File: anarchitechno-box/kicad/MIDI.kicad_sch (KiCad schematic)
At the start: 7 parts, among them CN1 PJ-3220-Y, U5 HCPL-0631

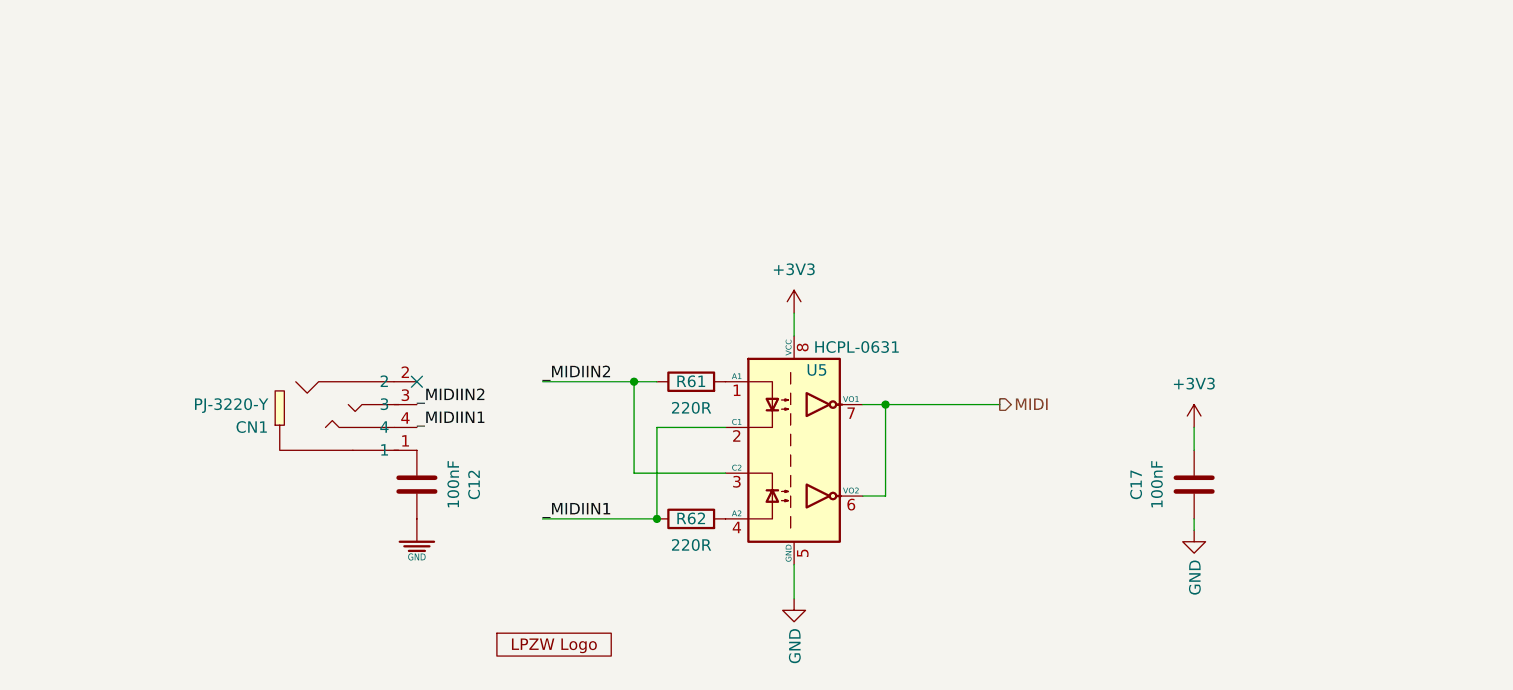
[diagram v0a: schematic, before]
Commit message: Schematic & PCB changes: - Cleaned up unnecessary electrolytic input capacitor flyback - Removed dual diode rectification on 5V, increased output capacitors - Feedback resistors DC/DCs set, enlarged for JLC basic parts - Sweep through schematic to consolidate caps to JLC basic parts (see list schematic front page) - Midi OUTPUT added (please check schematic) - Wiznet W5500 schematic reworked to RJ45 reference schematic: https://docs.wiznet.io/assets/files/w5500_sch_v110_use_mag_-dfff8bbb103d13be4f25cd2b2f8b950d.pdf - Replaced ethernet jack to HR911105A - Crystals chosen for W5500 and RP2350B (according to reference), 15pF load caps. - RS485 driver changed to SP3485EN for 3.3V operation - Replaced RS485 bus connectors with 2x RJ45s for passthrough - Groove connector replaced with JST XH 2mm - Added LCSC part numbers for various components in the schematic
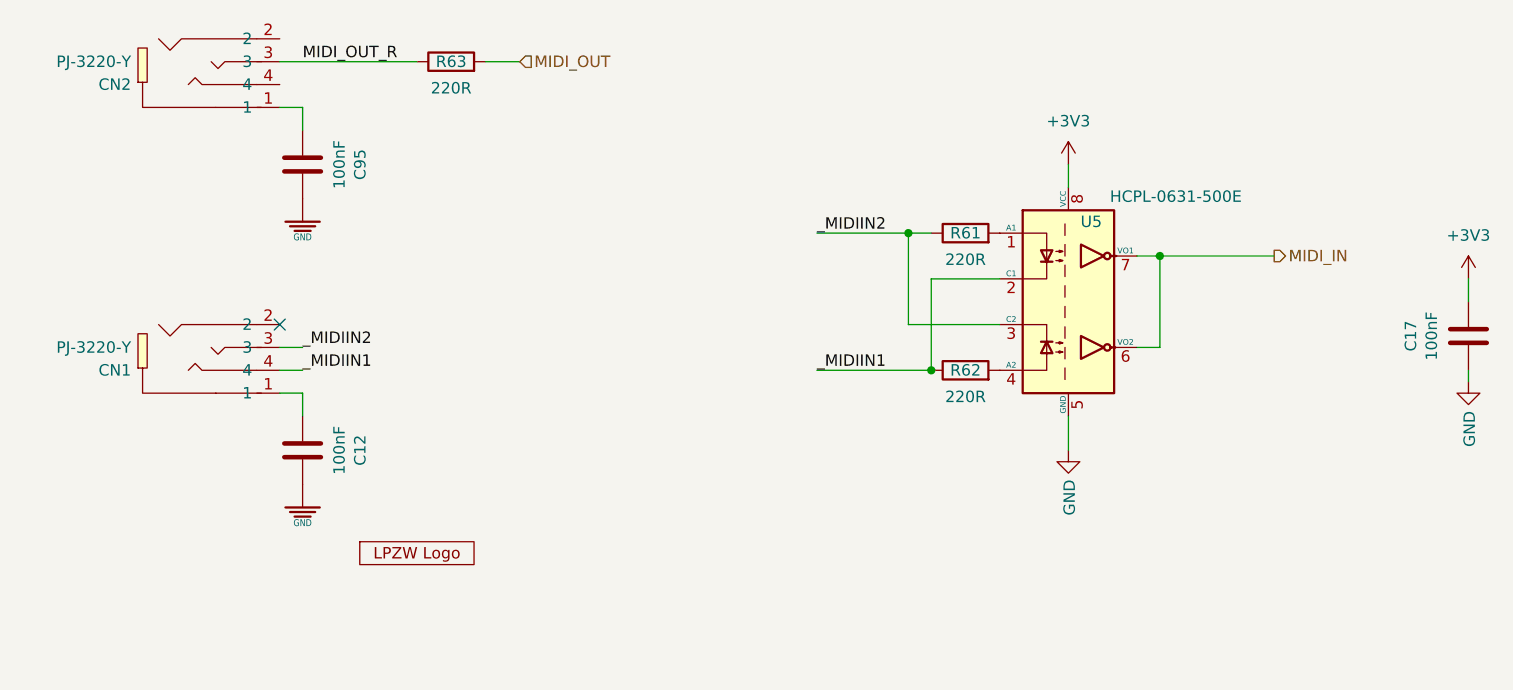
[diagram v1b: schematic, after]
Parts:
- added C95: 100nF, Capacitor_SMD:C_0402_1005Metric, symbol Device:C
- added CN2: PJ-3220-Y, parts:AUDIO-TH_PJ-3220-Y, symbol jlcpcb:PJ-3220-Y
- added R63: 220R, Resistor_SMD:R_0603_1608Metric, symbol Device:R
- CN1: footprint jlcpcb:AUDIO-TH_PJ-3220-Y -> parts:AUDIO-TH_PJ-3220-Y
- R61, R62: LCSC Part (none) -> C22962
- U5: value HCPL-0631 -> HCPL-0631-500E; LCSC Part (none) -> C43949
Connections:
- net GND: now also C95.1
- net MIDI renamed MIDI_IN
- new net: C95.2, CN2.1
- new net MIDI_OUT: R63.2
- new net MIDI_OUT_R: CN2.3, R63.1
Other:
- moved on the sheet: C12, C17, CN1, R61, R62, U5

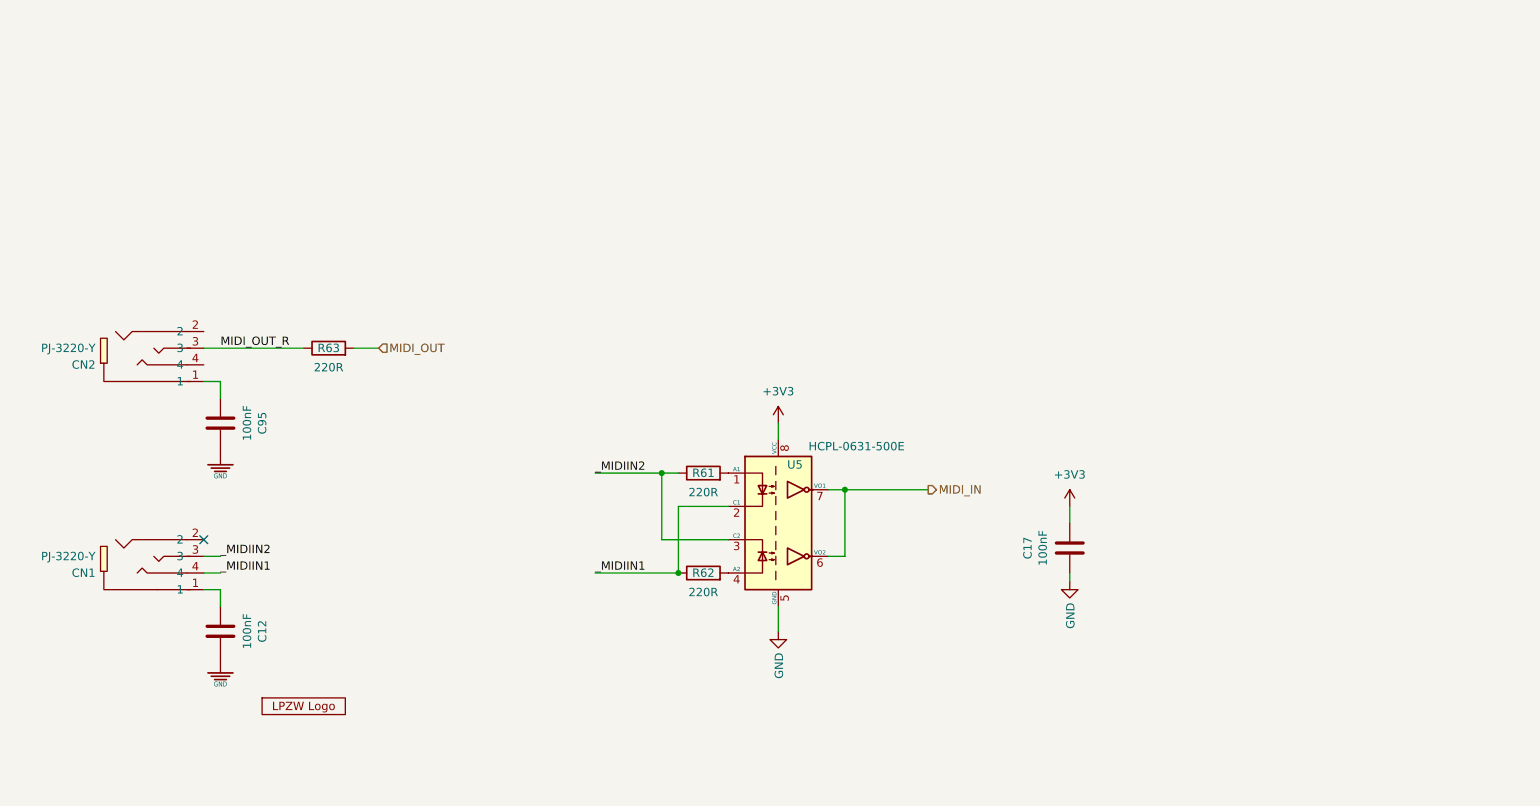
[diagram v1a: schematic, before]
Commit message: Midi output buffer
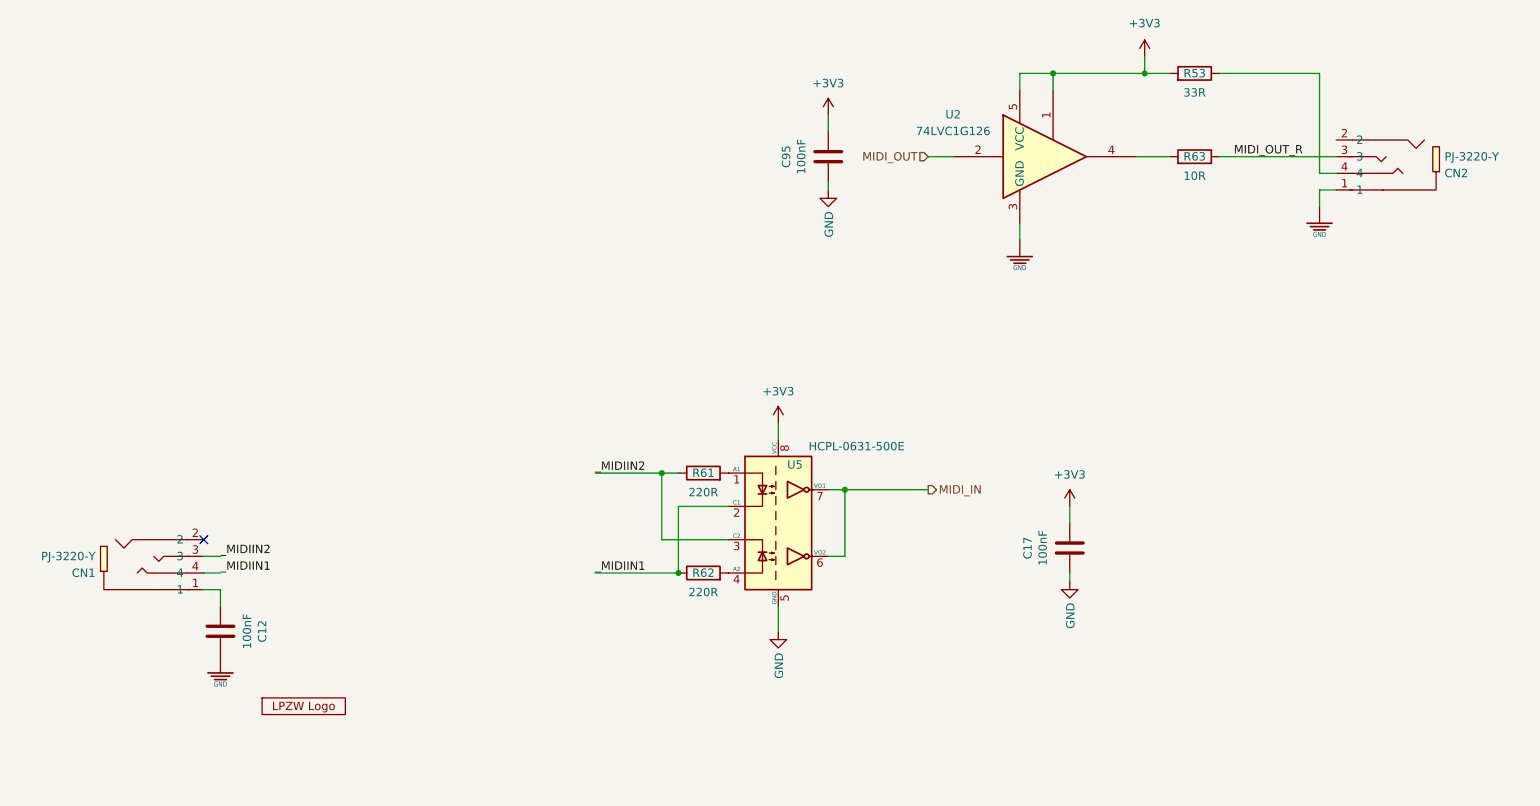
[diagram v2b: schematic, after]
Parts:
- added R53: 33R, Resistor_SMD:R_0603_1608Metric, symbol Device:R
- added U2: 74LVC1G126, Package_TO_SOT_SMD:SOT-23-5, symbol 74xGxx:74LVC1G126
- R63: value 220R -> 10R; LCSC Part C22962 -> (none)
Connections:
- net +3V3: now also C95.1, R53.2, U2.1, U2.5 (VCC)
- net GND: now also C95.2, CN2.1, U2.3 (GND); no longer C95.1
- net MIDI_OUT: now also U2.2; no longer R63.2
- net at CN2.4: now also R53.1
- new net: R63.2, U2.4
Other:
- moved on the sheet: CN2, R63

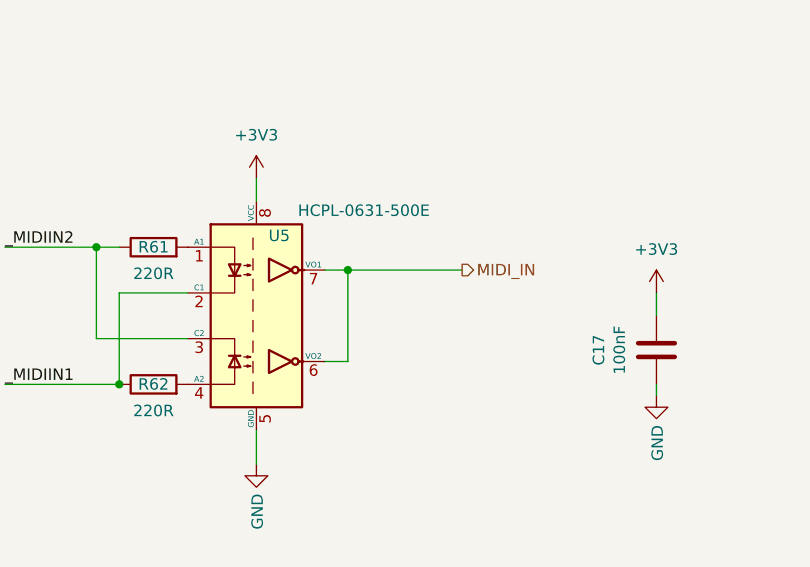
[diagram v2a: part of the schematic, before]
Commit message: - Logo Robot Theater lab - UART connector - RF antenne clearance aangepast - Reset/interrupt pins ethernet aangesloten
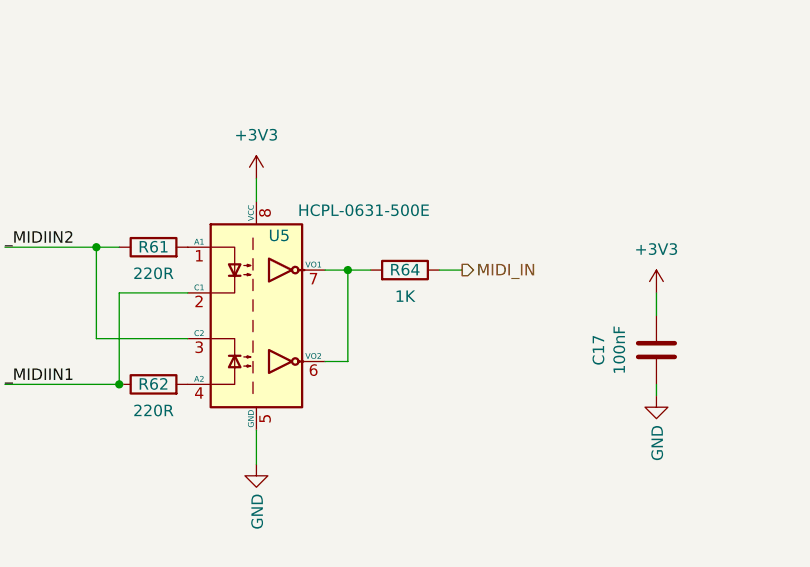
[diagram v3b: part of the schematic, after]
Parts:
- added R64: 1K, Resistor_SMD:R_0603_1608Metric, symbol Device:R
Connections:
- net MIDI_IN: now also R64.1; no longer U5.6 (VO2), U5.7 (VO1)
- new net: R64.2, U5.6 (VO2), U5.7 (VO1)
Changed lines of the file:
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@@
 	(wire
 		(pts
-			(xy 152.4 128.27) (xy 165.1 128.27)
+			(xy 152.4 128.27) (xy 154.94 128.27)
 		)
 		(stroke
@@
 		(pts
 			(xy 184.15 67.31) (xy 184.15 64.77)
+		)
+		(stroke
+			(width 0)
+			(type default)
+		)
+	)
+	(wire
+		(pts
+			(xy 162.56 128.27) (xy 165.1 128.27)
 		)
 		(stroke
@@
 					(unit 1)
 				)
+			)
+		)
+	)
+	(symbol
+		(lib_id "Device:R")
+		(at 158.75 128.27 270)
+		(mirror x)
+		(unit 1)
+		(exclude_from_sim no)
+		(in_bom yes)
+		(on_board yes)
+		(dnp no)
+		(property "Reference" "R64"
+			(at 158.75 128.27 90)
+			(effects
+				(font
+					(size 1.27 1.27)
+				)
+			)
+		)
+		(property "Value" "1K"
+			(at 158.75 131.2164 90)
+			(effects
+				(font
+					(size 1.27 1.27)
+				)
+			)
+		)
+		(property "Footprint" "Resistor_SMD:R_0603_1608Metric"
+			(at 158.75 130.048 90)
+			(effects
+				(font
+					(size 1.27 1.27)
+				)
+				(hide yes)
+			)
+		)
+		(property "Datasheet" "~"
+			(at 158.75 128.27 0)
+			(effects
+				(font
+					(size 1.27 1.27)
+				)
+				(hide yes)
+			)
+		)
+		(property "Description" ""
+			(at 158.75 128.27 0)
+			(effects
+				(font
+					(size 1.27 1.27)
+				)
+				(hide yes)
+			)
+		)
+		(property "LCSC Part" ""
+			(at 158.75 128.27 90)
+			(effects
+				(font
+					(size 1.27 1.27)
+				)
+				(hide yes)
+			)
+		)
+		(pin "1"
+		)
+		(pin "2"
+		)
+		(instances
+			(project "anarchytechnobox"
+				(path "/8c734c41-38ed-40fc-83bd-134786dcfb35/ffbe1760-7219-476c-a404-3e25c1e1c288"
+					(reference "R64")
+					(unit 1)
+				)

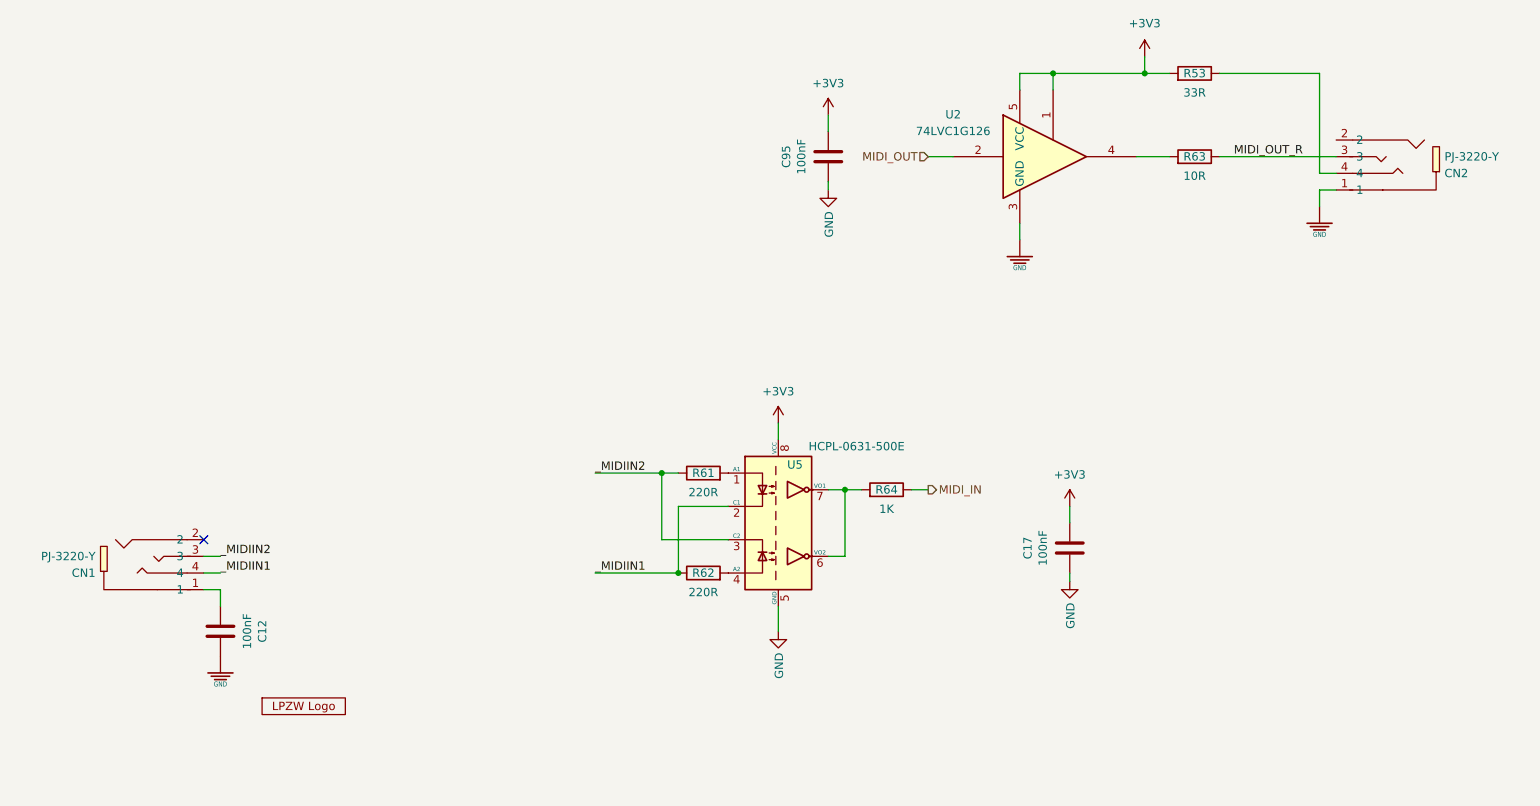
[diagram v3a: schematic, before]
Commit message: BOM nagelopen, bestelklaar.
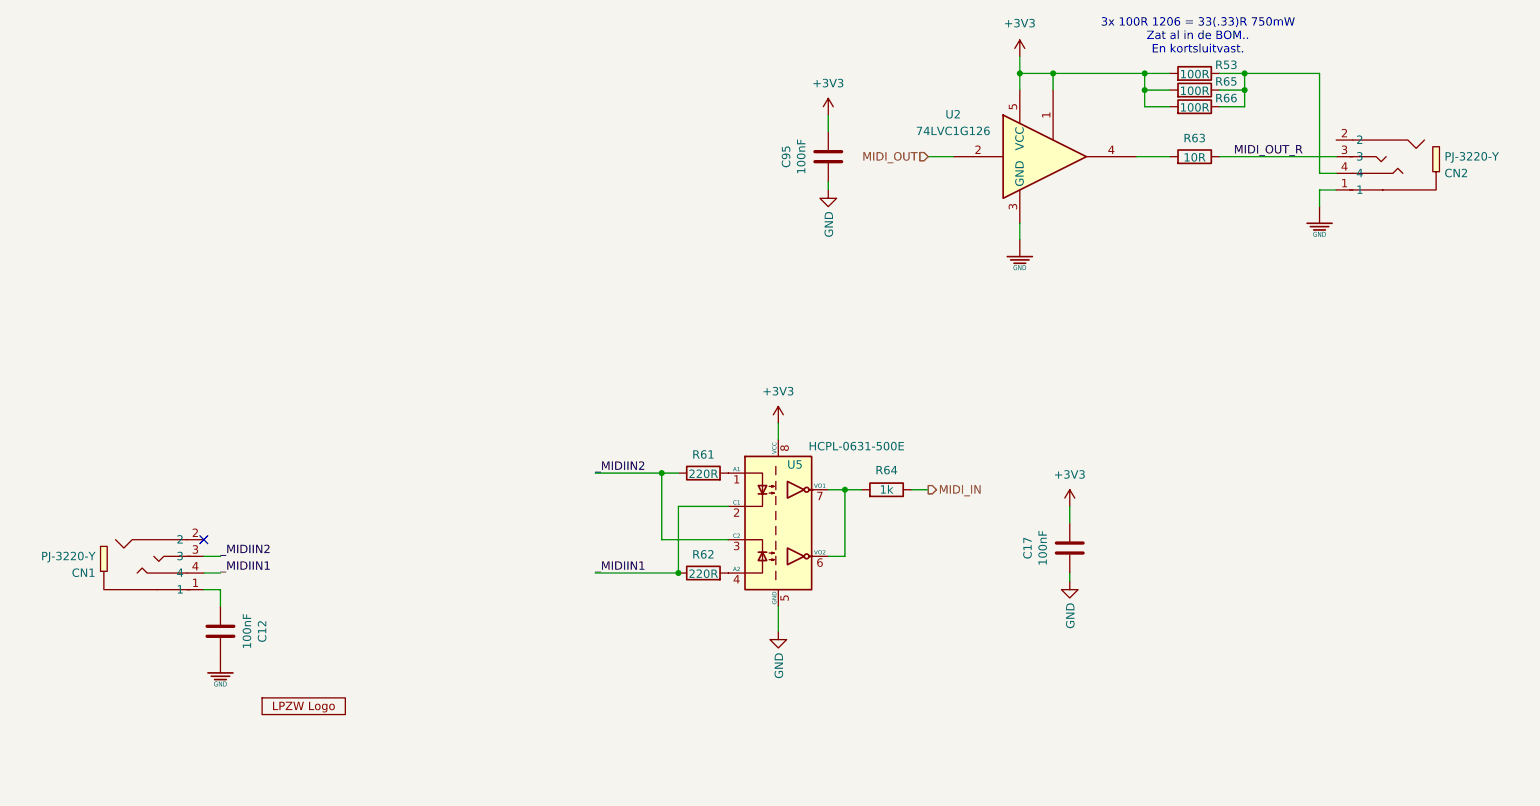
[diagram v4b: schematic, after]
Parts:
- added R65, R66: 100R, Resistor_SMD:R_1206_3216Metric, symbol Device:R
- R53: value 33R -> 100R; footprint Resistor_SMD:R_0603_1608Metric -> Resistor_SMD:R_1206_3216Metric
- R64: value 1K -> 1k
- U23: now left out of the parts list
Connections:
- net +3V3: now also R65.2, R66.2
- net at CN2.4, R53.1: now also R65.1, R66.1
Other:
- note added: "3x 100R 1206 = 33(.33)R 750mW Zat al in de BOM.. En kortsluitvast."
